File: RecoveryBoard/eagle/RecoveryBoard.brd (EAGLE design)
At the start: 120.9 x 54.6 mm, 96 parts, among them Q1 BSS123, Q2 BSS123, Q3 BSS123, Q4 BPR-301, Q5 BPR-301, Q6 MOSFET-PCH-SOT23-6, U1 STM32F042K6, U10 TPS63070, U2 BD62120AEFJ-E2, U3 H11F1SR2M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

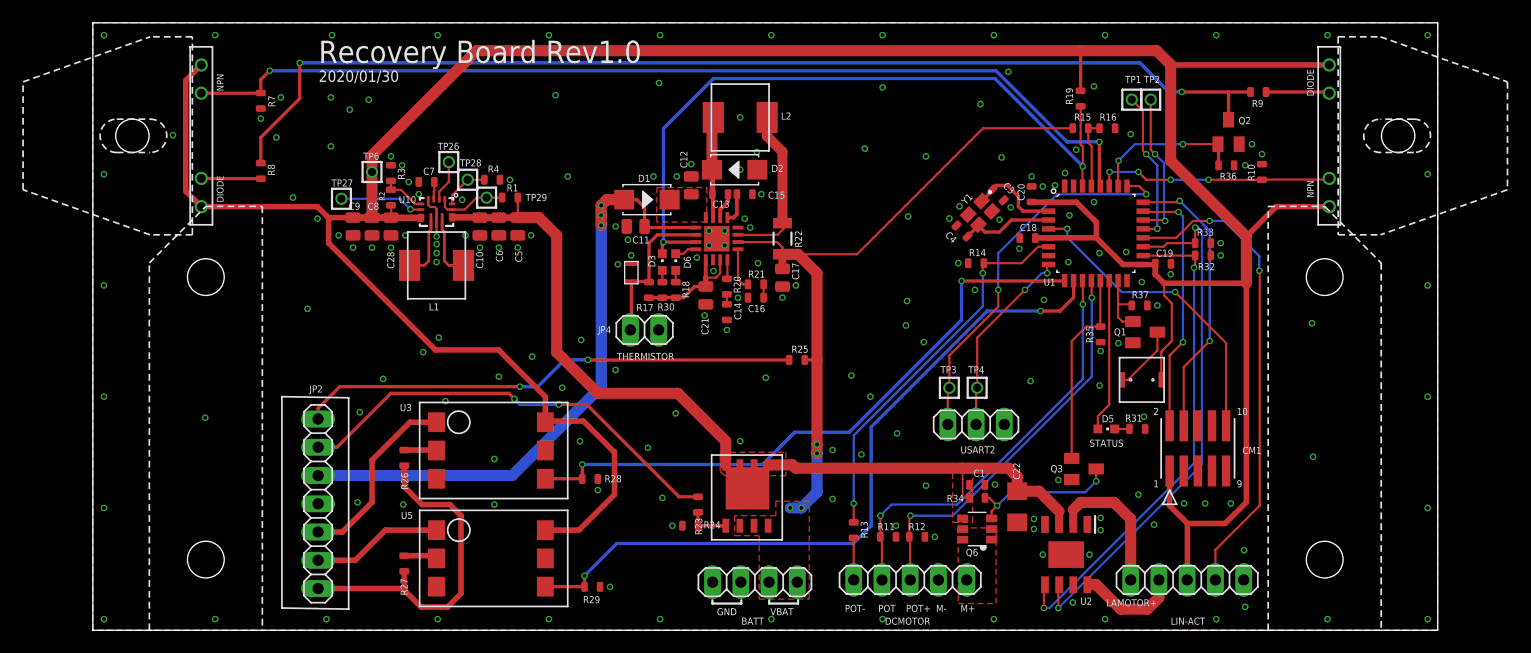
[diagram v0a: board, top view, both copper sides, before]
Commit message: fixed first round of issues with Rev1.0, and fixed some libraries as well
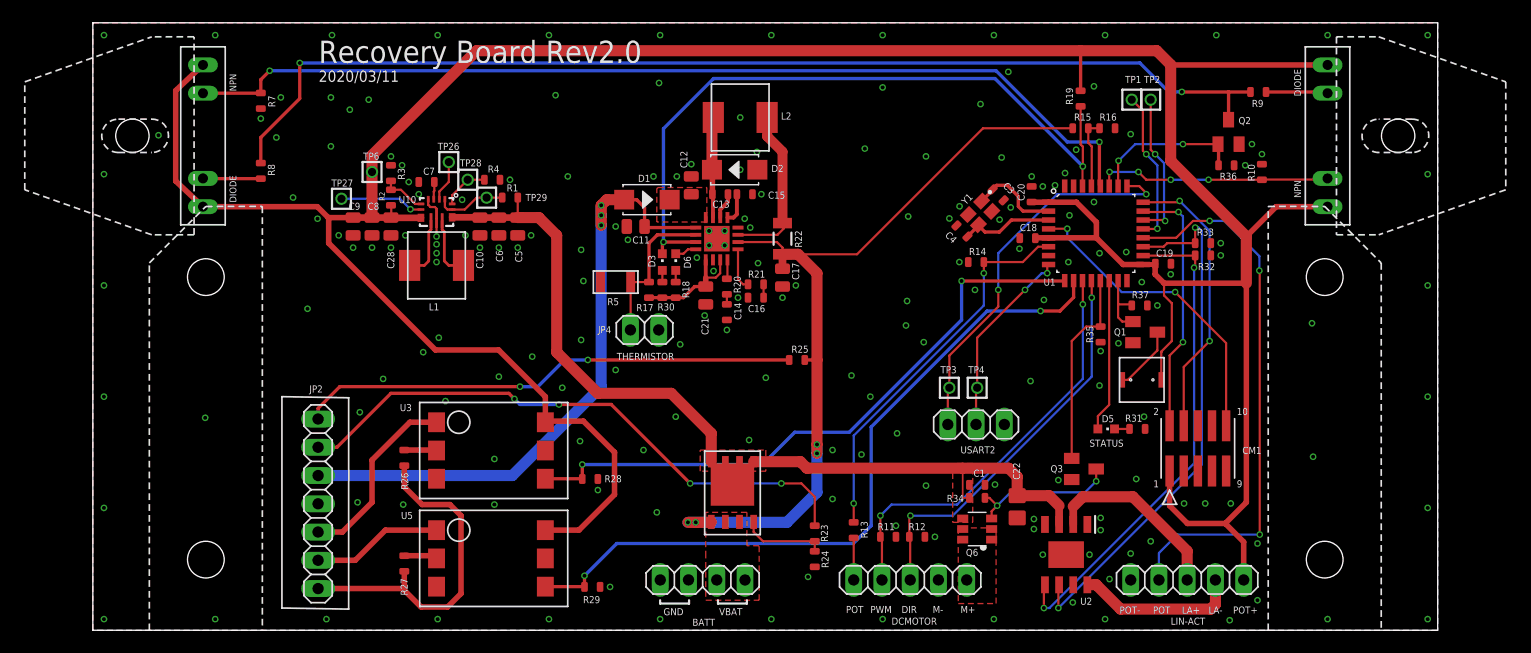
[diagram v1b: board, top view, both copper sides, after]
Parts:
- removed U$6: NHQ103B375T10, R--NHQ103B375T10--Thermistor:NHQ103B375T10
- removed U$8: SI7465DP, Q--Si7465DP--Vishay Power MOSFET with multple S+D leads:SI7465DP
- added Q7: SI7465DP-T1-E3, Q--Si7465DP--Vishay Power MOSFET with multple S+D leads:SI7465DP-T1-E3CT-ND
- added R5: (no value), R--NHQ103B375T10--Thermistor 10K:NHQ103B375T10
- C22: device oresat-rcl:C1206 -> oresat-rcl:.0805-A-NOSILK
- R8, R9: value 470 -> 220
- moved R24 11.6 mm to (64.9, 6.40), turned to 90 degrees
- moved R23 10.8 mm to (64.9, 8.70)
- moved JP1 4.70 mm to (54.8, 4.53)
- moved Q5 0.15 mm to (111.0, 44.5)
- moved Q4 0.15 mm to (9.90, 44.5)
- moved R14 0.10 mm to (79.4, 33.1)
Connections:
- net +12V: now also Q7.D1, Q7.D2, Q7.D3, Q7.D4, Q7.DPAD; no longer U$8.D, U$8.D1, U$8.D2, U$8.D3, U$8.D4
- net 3.3V: now also J2.5; no longer J2.3
- net GND: now also J2.1, R5.P2; no longer J2.5, U$6.P1
- net LAMOTOR+: now also J2.3; no longer J2.1
- net LAMOTOR-: now also J2.4; no longer J2.2
- net N$16: now also Q7.G; no longer U$8.G
- net N$20: now also R5.P1; no longer U$6.P2
- net POT_OUT_AN: now also J2.2; no longer J2.4
- net VBAT: now also Q7.S1, Q7.S2, Q7.S3; no longer U$8.S1, U$8.S2, U$8.S3
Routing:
- net ARM-IN: track 40.0 -> 53.1 mm, vias 2 -> 4
- net VBAT: track 63.9 -> 75.7 mm
- net POT_OUT_AN: track 43.2 -> 49.6 mm, vias 2 -> 3
- net LAMOTOR-: track 9.37 -> 14.8 mm
- net LAMOTOR+: track 12.9 -> 16.8 mm
- net N$16: track 4.40 -> 7.64 mm
- net 3.3V: track 289.8 -> 290.5 mm
- net +12V: track 76.1 -> 76.9 mm
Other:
- board text added: "2020/03/11"
- board text added: "DIR"
- board text added: "LA+"
- board text added: "LA-"
- board text added: "PWM"
- board text added: "Recovery Board Rev2.0"
- board text removed: "1. thermistor footprint is wrong - i recieved 1206 footprint 2. increase diameter of sensor holes 3. C22 footprint too big"
- board text removed: "2020/01/30"
- board text removed: "LAMOTOR+"
- board text removed: "Recovery Board Rev1.0"

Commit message: updated board with more test points, rearranged LA pins, and rearannged AI STM32 pins
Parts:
- added TP11, TP12, TP13, TP14, TP15, TP16, TP17, TP5, TP7, TP8: TEST-POINT, Tova:2MM-TEST-POINT
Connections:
- net IN1 renamed LA_IN1
- net IN2 renamed LA_IN2
- removed net POT_OUT_AN: J2.2, U1.20
- new net LA_POS: J2.2, TP8.1, U1.7
- net BATT_READ: now also U1.15; no longer U1.29
- net CHUTE: now also TP13.1
- net DROGUE: now also TP12.1
- net ISO-CHUTE: now also TP14.1
- net ISO-DROGUE: now also TP15.1
- net N$16: now also TP11.1
- net N$2: now also TP16.1
- net N$5: now also TP17.1
- net SENSOR1: now also TP5.1
- net SENSOR2: now also TP7.1
- net SPKR: now also U1.20; no longer U1.15
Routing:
- net POT_OUT_AN: track 49.6 -> 0.00 mm, vias 3 -> 0
- net LA_POS: track 0.00 -> 39.7 mm, vias 0 -> 4
- net BATT_READ: track 6.35 -> 15.9 mm, vias 0 -> 2
- net SPKR: track 6.06 -> 13.0 mm, vias 0 -> 2
- net N$5: track 5.69 -> 8.38 mm
- net USART2_RX: track 34.9 -> 32.3 mm
- net N$16: track 7.64 -> 10.1 mm
- net N$2: track 5.46 -> 6.96 mm
- net SENSOR2: track 21.3 -> 22.7 mm
- net USART2_TX: track 17.4 -> 18.3 mm
- net SENSOR1: vias 2 -> 1

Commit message: finishing routing for REV 2.0
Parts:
- removed R13: 1.8k, oresat-rcl:.0603-C-NOSILK
- removed R14: 3.3k, oresat-rcl:.0603-C-NOSILK
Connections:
- removed net PULSEOUT: J1.5, R13.1
- net DCM_SPEED: now also J1.5; no longer R13.2, R14.1
- net GND: no longer R14.2
- net SPKR: now also U1.31; no longer U1.20
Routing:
- net SPKR: track 13.0 -> 28.5 mm, vias 2 -> 6
- net DCM_SPEED: track 34.6 -> 44.6 mm
- net PULSEOUT: track 3.78 -> 0.00 mm
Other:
- board text added: "FG"
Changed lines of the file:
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@@
 <drawing>
 <settings>
-<setting alwaysvectorfont="yes"/>
+<setting alwaysvectorfont="no"/>
 <setting verticaltext="up"/>
 </settings>
@@
 <text x="75.5" y="1.55" size="0.635" layer="21" font="vector" ratio="20">M-</text>
 <text x="69.9" y="1.55" size="0.635" layer="21" font="vector" ratio="20">PWM</text>
-<text x="67.7" y="1.55" size="0.635" layer="21" font="vector" ratio="20">POT</text>
+<text x="67.7" y="1.55" size="0.635" layer="21" font="vector" ratio="20">FG</text>
 <text x="89.6" y="16.5" size="0.635" layer="21" font="vector" ratio="20">STATUS</text>
 <text x="100.3" y="1.5" size="0.635" layer="21" font="vector" ratio="20">LA-</text>
@@
 <attribute name="VALUE" x="73.465" y="6.495" size="0.4064" layer="27"/>
 </element>
-<element name="R13" library="oresat-rcl" package=".0603-C-NOSILK" value="1.8k" x="68.4" y="9" smashed="yes" rot="R90">
-<attribute name="NAME" x="69.665" y="8.265" size="0.635" layer="25" font="vector" ratio="20" rot="R90"/>
-<attribute name="VALUE" x="70.305" y="8.365" size="0.4064" layer="27" rot="R90"/>
-</element>
-<element name="R14" library="oresat-rcl" package=".0603-C-NOSILK" value="3.3k" x="79.4" y="33.1" smashed="yes" rot="R180">
-<attribute name="NAME" x="78.765" y="33.735" size="0.635" layer="25" font="vector" ratio="20"/>
-<attribute name="VALUE" x="78.035" y="34.005" size="0.4064" layer="27" rot="R180"/>
-</element>
 <element name="R15" library="oresat-rcl" package=".0603-C-NOSILK" value="27k" x="88.79" y="45.13" smashed="yes" rot="R180">
 <attribute name="DIS" value="Digi-Key" x="54.5" y="109.9" size="1.778" layer="27" rot="R180" display="off"/>
@@
 <contactref element="R12" pad="2"/>
 <contactref element="R11" pad="2"/>
-<contactref element="R14" pad="2"/>
 <contactref element="R28" pad="2"/>
 <contactref element="C18" pad="2"/>
@@
 <via x="84.4" y="40.8" extent="1-16" drill="0.35"/>
 <via x="85.4" y="39.9" extent="1-16" drill="0.35"/>
-<via x="86.5" y="40" extent="1-16" drill="0.35"/>
+<via x="86.3" y="41.1" extent="1-16" drill="0.35"/>
 <via x="81.51629375" y="36.91213125" extent="1-16" drill="0.35"/>
 <via x="77.91629375" y="38.11213125" extent="1-16" drill="0.35"/>
@@
 <wire x1="55.595" y1="17.905" x2="55.595" y2="17.795" width="1" layer="1"/>
 <wire x1="55.595" y1="17.795" x2="55.595" y2="15.155" width="1" layer="1"/>
-<wire x1="78.8" y1="11.9" x2="78.8" y2="13.07" width="0" layer="19" extent="1-1"/>
-<wire x1="58.135" y1="15.155" x2="59.405" y2="15.155" width="0" layer="19" extent="1-1"/>
-<wire x1="56.865" y1="15.155" x2="58.135" y2="15.155" width="0" layer="19" extent="1-1"/>
-<wire x1="55.595" y1="15.155" x2="56.865" y2="15.155" width="0" layer="19" extent="1-1"/>
-<wire x1="78.2" y1="10.05" x2="78.2" y2="11.9" width="0" layer="19" extent="1-1"/>
-<wire x1="57.5" y1="13.1" x2="58.135" y2="15.155" width="0" layer="19" extent="1-1"/>
 </signal>
 <signal name="CHUTE">
@@
 <wire x1="89.3" y1="27.3" x2="88" y2="26" width="0.2" layer="1"/>
 <wire x1="88" y1="26" x2="88" y2="15.45" width="0.2" layer="1"/>
-</signal>
-<signal name="PULSEOUT">
-<contactref element="J1" pad="5"/>
-<contactref element="R13" pad="1"/>
-<wire x1="68.4" y1="8.3" x2="68.4" y2="4.525" width="0.2" layer="1"/>
-</signal>
-<signal name="DCM_SPEED">
-<contactref element="R14" pad="1"/>
-<contactref element="R13" pad="2"/>
-<contactref element="U1" pad="6"/>
-<wire x1="68.4" y1="11.4" x2="68.4" y2="9.7" width="0.2" layer="1"/>
-<via x="68.4" y="11.4" extent="1-16" drill="0.35"/>
-<wire x1="68.4" y1="11.4" x2="68.4" y2="17.5" width="0.2" layer="16"/>
-<wire x1="80.1" y1="29.2" x2="68.4" y2="17.5" width="0.2" layer="16"/>
-<wire x1="80.1" y1="29.2" x2="80.1" y2="32.1" width="0.2" layer="16"/>
-<via x="80.1" y="32.1" extent="1-16" drill="0.35"/>
-<wire x1="80.1" y1="32.1" x2="80.1" y2="33.1" width="0.2" layer="1"/>
-<wire x1="80.1" y1="33.1" x2="83.6" y2="33.1" width="0.2" layer="1"/>
-<wire x1="84.98" y1="34.48" x2="85.92" y2="34.48" width="0.2" layer="1"/>
-<wire x1="83.6" y1="33.1" x2="84.98" y2="34.48" width="0.2" layer="1"/>
 </signal>
 <signal name="CAN_RX">
@@
 <wire x1="55.555" y1="9.7" x2="55.595" y2="9.74" width="1" layer="1"/>
 <via x="54.2" y="9.7" extent="1-16" drill="0.35"/>
-<wire x1="58.135" y1="9.74" x2="56.865" y2="9.74" width="0" layer="19" extent="1-1"/>
-<wire x1="55.595" y1="9.74" x2="56.865" y2="9.74" width="0" layer="19" extent="1-1"/>
-<wire x1="56.09" y1="4.525" x2="55.555" y2="9.7" width="0" layer="19" extent="1-1"/>
-<wire x1="58.63" y1="4.525" x2="56.09" y2="4.525" width="0" layer="19" extent="1-1"/>
 </signal>
 <signal name="N$22">
@@
 <wire x1="92.17" y1="29.3" x2="92.17" y2="28.13" width="0.2" layer="1"/>
 <wire x1="92.17" y1="28.13" x2="92.55" y2="27.75" width="0.2" layer="1"/>
-<contactref element="U1" pad="20"/>
-<wire x1="94.42" y1="35.28" x2="95.92" y2="35.28" width="0.2" layer="1"/>
-<wire x1="95.92" y1="35.28" x2="96" y2="35.2" width="0.2" layer="1"/>
-<via x="96" y="35.2" extent="1-16" drill="0.35"/>
-<wire x1="96" y1="35.2" x2="96" y2="32.1" width="0.2" layer="16"/>
-<wire x1="96" y1="32.1" x2="95.2" y2="31.3" width="0.2" layer="16"/>
+<wire x1="95.2" y1="31.3" x2="96" y2="32.1" width="0.2" layer="16"/>
 <via x="95.2" y="31.3" extent="1-16" drill="0.35"/>
 <wire x1="95.2" y1="31.3" x2="94.5" y2="30.6" width="0.2" layer="1"/>
@@
 <wire x1="93.9" y1="30.6" x2="93.4" y2="30.1" width="0.2" layer="1"/>
 <wire x1="93.4" y1="30.1" x2="93.4" y2="29.2" width="0.2" layer="1"/>
+<contactref element="U1" pad="31"/>
+<wire x1="88.17" y1="39.93" x2="88.17" y2="41.47" width="0.2" layer="1"/>
+<wire x1="88.17" y1="41.47" x2="88.2" y2="41.5" width="0.2" layer="1"/>
+<wire x1="96" y1="35.3" x2="97.0456" y2="36.3456" width="0.2" layer="16"/>
+<via x="97" y="39.5" extent="1-16" drill="0.35"/>
+<wire x1="97.0456" y1="36.3456" x2="97.0456" y2="39.4544" width="0.2" layer="16"/>
+<wire x1="97" y1="39.5" x2="97.0456" y2="39.4544" width="0.2" layer="16"/>
+<wire x1="96" y1="32.1" x2="96" y2="35.3" width="0.2" layer="16"/>
+<wire x1="97" y1="39.5" x2="94.1" y2="39.5" width="0.2" layer="1"/>
+<via x="94.1" y="39.5" extent="1-16" drill="0.35"/>
+<wire x1="94.1" y1="39.5" x2="92.8" y2="39.5" width="0.2" layer="16"/>
+<wire x1="92.8" y1="39.5" x2="91.9" y2="38.6" width="0.2" layer="16"/>
+<via x="91.9" y="38.6" extent="1-16" drill="0.35"/>
+<wire x1="91.9" y1="38.6" x2="91.8" y2="38.7" width="0.2" layer="1"/>
+<wire x1="91.8" y1="38.7" x2="90.3" y2="38.7" width="0.2" layer="1"/>
+<via x="90.3" y="38.7" extent="1-16" drill="0.35"/>
+<wire x1="90.3" y1="38.7" x2="88.17" y2="40.83" width="0.2" layer="16"/>
+<wire x1="88.17" y1="40.83" x2="88.17" y2="41.47" width="0.2" layer="16"/>
+<via x="88.17" y="41.47" extent="1-16" drill="0.35"/>
 </signal>
 <signal name="LED">
@@
 <via x="91.4" y="4.6" extent="1-16" drill="0.35"/>
 </signal>
+<signal name="DCM_SPEED">
+<contactref element="J1" pad="5"/>
+<contactref element="U1" pad="6"/>
+<wire x1="85.92" y1="34.48" x2="84.98" y2="34.48" width="0.2" layer="1"/>
+<wire x1="68.3" y1="29.3" x2="68.3" y2="16.9" width="0.2" layer="1"/>
+<via x="68.3" y="16.9" extent="1-16" drill="0.35"/>
+<wire x1="68.3" y1="16.9" x2="68.3" y2="12.7" width="0.2" layer="16"/>
+<wire x1="68.3" y1="12.7" x2="68.3" y2="9.9" width="0.2" layer="16"/>
+<wire x1="68.3" y1="9.9" x2="68.4" y2="9.8" width="0.2" layer="16"/>
+<via x="68.4" y="9.8" extent="1-16" drill="0.35"/>
+<wire x1="68.4" y1="9.8" x2="68.4" y2="4.525" width="0.2" layer="1"/>
+<wire x1="84.98" y1="34.48" x2="82.8" y2="32.3" width="0.2" layer="1"/>
+<wire x1="82.8" y1="32.3" x2="71.3" y2="32.3" width="0.2" layer="1"/>
+<wire x1="71.3" y1="32.3" x2="68.3" y2="29.3" width="0.2" layer="1"/>
+</signal>
 </signals>
